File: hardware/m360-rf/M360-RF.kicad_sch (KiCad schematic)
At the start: 5 parts, among them J1 M360-RF 2x5, J2 SMA borda, U1 RFM95W-915S2

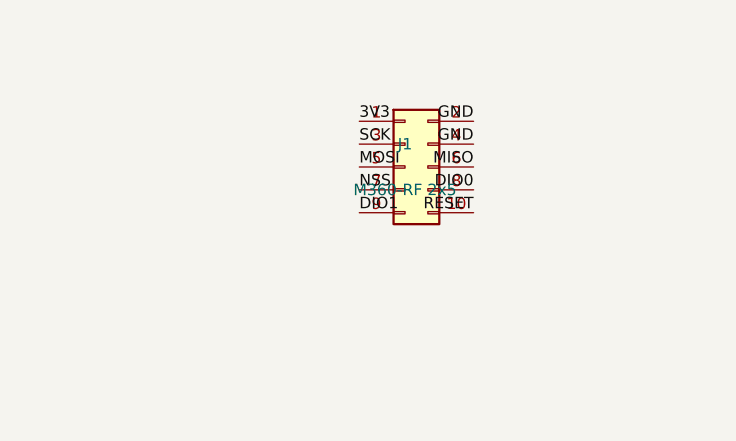
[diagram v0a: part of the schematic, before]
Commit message: feat(hardware): layout da placa do mezanino M360-RF
Placa de 34,2 x 23 mm, 2 camadas, 1,6 mm. RFM95W no centro; header 2x5 na face de baixo, à esquerda; SMA Samtec na borda direita, alinhado ao pino ANA. Trilha de RF coplanar com terra (1,25 mm, gap 0,2 mm, ~5 mm). SPI reto até a coluna de dentro do header; DIO1, DIO0 e 3V3 contornam o rádio por cima, em F.Cu, sem cruzamentos. GND nas duas faces com 17 vias de costura, nenhuma sob o módulo. Referências de C1, C2 e J2 ocultas na serigrafia.

Pinagem do header reordenada para o layout (MISO/MOSI/SCK/NSS/RESET na coluna ímpar, DIO1/DIO0/3V3/GND/GND na par); esquemático religado e ERC sem violações. DRC do kicad-cli: 0 violações, 0 itens desconectados, 0 divergências com o esquemático. ARQUITETURA_FAMILIA.md: nova pinagem e interface mecânica do mezanino para os carriers.

Co-Authored-By: Claude Opus 5 (1M context) <noreply@anthropic.com>

Claude-Session: https://claude.ai/code/session_01G3CpSsqAsoKgMUYE5MhRV7
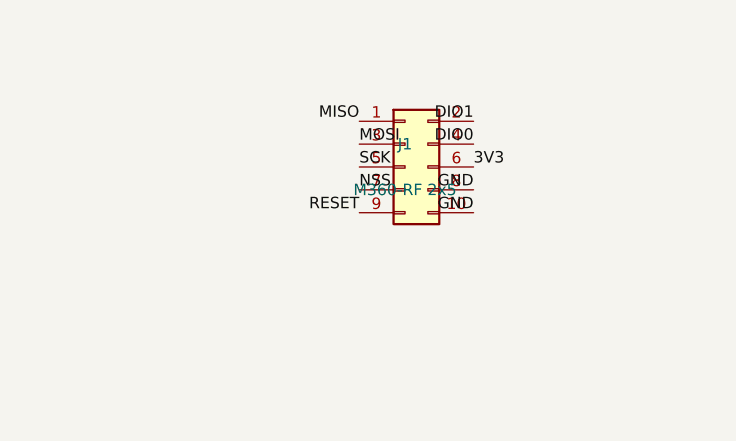
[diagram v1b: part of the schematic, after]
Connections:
- net 3V3: now also J1.6 (Pin_6); no longer J1.1 (Pin_1)
- net DIO0: now also J1.4 (Pin_4); no longer J1.8 (Pin_8)
- net DIO1: now also J1.2 (Pin_2); no longer J1.9 (Pin_9)
- net GND: now also J1.10 (Pin_10), J1.8 (Pin_8); no longer J1.2 (Pin_2), J1.4 (Pin_4)
- net MISO: now also J1.1 (Pin_1); no longer J1.6 (Pin_6)
- net MOSI: now also J1.3 (Pin_3); no longer J1.5 (Pin_5)
- net RESET: now also J1.9 (Pin_9); no longer J1.10 (Pin_10)
- net SCK: now also J1.5 (Pin_5); no longer J1.3 (Pin_3)
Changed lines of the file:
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@@
 			)
 		)
-    (property "MPN" "RFM95W-915S2" (at 110.49 90.17 0)
-      (effects (font (size 1.27 1.27)) (hide yes))
-    )
-    (property "Manufacturer" "HopeRF" (at 110.49 90.17 0)
-      (effects (font (size 1.27 1.27)) (hide yes))
-    )
-    (property "Montagem" "Manual: modulo HopeRF do estoque proprio, nao montar na PCBA" (at 110.49 90.17 0)
-      (effects (font (size 1.27 1.27)) (hide yes))
-    )
+		(property "MPN" "RFM95W-915S2"
+			(at 110.49 90.17 0)
+			(effects
+				(font
+					(size 1.27 1.27)
+				)
+				(hide yes)
+			)
+		)
+		(property "Manufacturer" "HopeRF"
+			(at 110.49 90.17 0)
+			(effects
+				(font
+					(size 1.27 1.27)
+				)
+				(hide yes)
+			)
+		)
+		(property "Montagem" "Manual: modulo HopeRF do estoque proprio, nao montar na PCBA"
+			(at 110.49 90.17 0)
+			(effects
+				(font
+					(size 1.27 1.27)
+				)
+				(hide yes)
+			)
+		)
 		(pin "1"
 		)
@@
 			)
 		)
-    (property "LCSC" "C492422" (at 175.26 90.17 0)
-      (effects (font (size 1.27 1.27)) (hide yes))
-    )
-    (property "Montagem" "Manual: header THT soldado apos a PCBA" (at 175.26 90.17 0)
-      (effects (font (size 1.27 1.27)) (hide yes))
-    )
+		(property "LCSC" "C492422"
+			(at 175.26 90.17 0)
+			(effects
+				(font
+					(size 1.27 1.27)
+				)
+				(hide yes)
+			)
+		)
+		(property "Montagem" "Manual: header THT soldado apos a PCBA"
+			(at 175.26 90.17 0)
+			(effects
+				(font
+					(size 1.27 1.27)
+				)
+				(hide yes)
+			)
+		)
 		(pin "1"
 		)
@@
 			)
 		)
-    (property "LCSC" "C5199907" (at 59.69 85.09 0)
-      (effects (font (size 1.27 1.27)) (hide yes))
-    )
-    (property "MPN" "SMA-J-P-H-ST-EM1" (at 59.69 85.09 0)
-      (effects (font (size 1.27 1.27)) (hide yes))
-    )
-    (property "Manufacturer" "Samtec" (at 59.69 85.09 0)
-      (effects (font (size 1.27 1.27)) (hide yes))
-    )
+		(property "LCSC" "C5199907"
+			(at 59.69 85.09 0)
+			(effects
+				(font
+					(size 1.27 1.27)
+				)
+				(hide yes)
+			)
+		)
+		(property "MPN" "SMA-J-P-H-ST-EM1"
+			(at 59.69 85.09 0)
+			(effects
+				(font
+					(size 1.27 1.27)
+				)
+				(hide yes)
+			)
+		)
+		(property "Manufacturer" "Samtec"
+			(at 59.69 85.09 0)
+			(effects
+				(font
+					(size 1.27 1.27)
+				)
+				(hide yes)
+			)
+		)
 		(pin "1"
 		)
@@
 			)
 		)
-    (property "LCSC" "C14663" (at 134.62 129.54 0)
-      (effects (font (size 1.27 1.27)) (hide yes))
-    )
+		(property "LCSC" "C14663"
+			(at 134.62 129.54 0)
+			(effects
+				(font
+					(size 1.27 1.27)
+				)
+				(hide yes)
+			)
+		)
 		(pin "1"
 		)
@@
 			)
 		)
-    (property "LCSC" "C45783" (at 149.86 129.54 0)
-      (effects (font (size 1.27 1.27)) (hide yes))
-    )
+		(property "LCSC" "C45783"
+			(at 149.86 129.54 0)
+			(effects
+				(font
+					(size 1.27 1.27)
+				)
+				(hide yes)
+			)
+		)
 		(pin "1"
 		)
@@
 		)
 	)
+	(label "RF_ANT"
+		(at 54.61 85.09 0)
+		(effects
+			(font
+				(size 1.27 1.27)
+			)
+			(justify left bottom)
+		)
+	)
+	(label "GND"
+		(at 59.69 90.17 90)
+		(effects
+			(font
+				(size 1.27 1.27)
+			)
+			(justify left bottom)
+		)
+	)
 	(label "3V3"
-		(at 170.17999999999998 85.09 0)
-		(effects
-			(font
-				(size 1.27 1.27)
-			)
-			(justify left bottom)
+		(at 134.62 125.72999999999999 270)
+		(effects
+			(font
+				(size 1.27 1.27)
+			)
+			(justify right bottom)
 		)
 	)
 	(label "GND"
+		(at 134.62 133.35 90)
+		(effects
+			(font
+				(size 1.27 1.27)
+			)
+			(justify left bottom)
+		)
+	)
+	(label "3V3"
+		(at 149.86 125.72999999999999 270)
+		(effects
+			(font
+				(size 1.27 1.27)
+			)
+			(justify right bottom)
+		)
+	)
+	(label "GND"
+		(at 149.86 133.35 90)
+		(effects
+			(font
+				(size 1.27 1.27)
+			)
+			(justify left bottom)
+		)
+	)
+	(label "3V3"
+		(at 190.5 129.54 90)
+		(effects
+			(font
+				(size 1.27 1.27)
+			)
+			(justify left bottom)
+		)
+	)
+	(label "GND"
+		(at 204.47 129.54 90)
+		(effects
+			(font
+				(size 1.27 1.27)
+			)
+			(justify left bottom)
+		)
+	)
+	(no_connect
+		(at 123.19 87.63)
+	)
+	(no_connect
+		(at 123.19 92.71000000000001)
+	)
+	(no_connect
+		(at 123.19 90.17)
+	)
+	(no_connect
+		(at 123.19 95.25)
+	)
+	(label "DIO1"
 		(at 182.88 85.09 180)
 		(effects
@@
 		)
 	)
+	(label "MOSI"
+		(at 170.17999999999998 87.63 0)
+		(effects
+			(font
+				(size 1.27 1.27)
+			)
+			(justify left bottom)
+		)
+	)
+	(label "DIO0"
+		(at 182.88 87.63 180)
+		(effects
+			(font
+				(size 1.27 1.27)
+			)
+			(justify right bottom)
+		)
+	)
 	(label "SCK"
-		(at 170.17999999999998 87.63 0)
-		(effects
-			(font
-				(size 1.27 1.27)
-			)
-			(justify left bottom)
-		)
-	)
-	(label "GND"
-		(at 182.88 87.63 180)
-		(effects
-			(font
-				(size 1.27 1.27)
-			)
-			(justify right bottom)
-		)
-	)
-	(label "MOSI"
 		(at 170.17999999999998 90.17 0)
 		(effects
@@
 			)
 			(justify left bottom)
-		)
-	)
-	(label "MISO"
-		(at 182.88 90.17 180)
-		(effects
-			(font
-				(size 1.27 1.27)
-			)
-			(justify right bottom)
 		)
 	)
@@
 		)
 	)
-	(label "DIO0"
+	(label "GND"
 		(at 182.88 92.71000000000001 180)
 		(effects
@@
 		)
 	)
-	(label "DIO1"
-		(at 170.17999999999998 95.25 0)
+	(label "GND"
+		(at 182.88 95.25 180)
+		(effects
+			(font
+				(size 1.27 1.27)
+			)
+			(justify right bottom)
+		)
+	)
+	(label "MISO"
+		(at 170.17999999999998 85.09 180)
+		(effects
+			(font
+				(size 1.27 1.27)
+			)
+			(justify right bottom)
+		)
+	)
+	(label "3V3"
+		(at 182.88 90.17 0)
 		(effects
 			(font
@@
 	)
 	(label "RESET"
-		(at 182.88 95.25 180)
-		(effects
-			(font
-				(size 1.27 1.27)
-			)
-			(justify right bottom)
-		)
-	)
-	(label "RF_ANT"
-		(at 54.61 85.09 0)
-		(effects
-			(font
-				(size 1.27 1.27)
-			)
-			(justify left bottom)
-		)
-	)
-	(label "GND"
-		(at 59.69 90.17 90)
-		(effects
-			(font
-				(size 1.27 1.27)
-			)
-			(justify left bottom)
-		)
-	)
-	(label "3V3"
-		(at 134.62 125.72999999999999 270)
-		(effects
-			(font
-				(size 1.27 1.27)
-			)
-			(justify right bottom)
-		)
-	)
-	(label "GND"
-		(at 134.62 133.35 90)
-		(effects
-			(font
-				(size 1.27 1.27)
-			)
-			(justify left bottom)
-		)
-	)
-	(label "3V3"
-		(at 149.86 125.72999999999999 270)
-		(effects
-			(font
-				(size 1.27 1.27)
-			)
-			(justify right bottom)
-		)
-	)
-	(label "GND"
-		(at 149.86 133.35 90)
-		(effects
-			(font
-				(size 1.27 1.27)
-			)
-			(justify left bottom)
-		)
-	)
-	(label "3V3"
-		(at 190.5 129.54 90)
-		(effects
-			(font
-				(size 1.27 1.27)
-			)
-			(justify left bottom)
-		)
-	)
-	(label "GND"
-		(at 204.47 129.54 90)
-		(effects
-			(font
-				(size 1.27 1.27)
-			)
-			(justify left bottom)
-		)
-	)
-	(no_connect
-		(at 123.19 87.63)
-	)
-	(no_connect
-		(at 123.19 92.71000000000001)
-	)
-	(no_connect
-		(at 123.19 90.17)
-	)
-	(no_connect
-		(at 123.19 95.25)
+		(at 170.17999999999998 95.25 180)
+		(effects
+			(font
+				(size 1.27 1.27)
+			)
+			(justify right bottom)
+		)
 	)
 	(sheet_instances

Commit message: feat(hardware): arquivos de fabricação da M360-RF
- U1 (RFM95W) e J1 (header 2x5, face de baixo) marcados como solda manual,
  fora do BOM e da posição; netdiff e paridade idênticos
- fabricacao/: C1, C2 e o SMA de borda J2, todos com LCSC
- §8: lista de solda manual das quatro placas

ERC 0, DRC --severity-all 0/0.

Co-Authored-By: Claude Opus 5 (1M context) <noreply@anthropic.com>
Claude-Session: https://claude.ai/code/session_012t7RkcrXvvpDVjKVimNu18
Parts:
- J1, U1: now left out of the parts list
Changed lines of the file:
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@@
 		(body_style 1)
 		(exclude_from_sim no)
-		(in_bom yes)
+		(in_bom no)
 		(on_board yes)
-		(in_pos_files yes)
+		(in_pos_files no)
 		(dnp no)
 		(property "Reference" "U1"
@@
 		(body_style 1)
 		(exclude_from_sim no)
-		(in_bom yes)
+		(in_bom no)
 		(on_board yes)
-		(in_pos_files yes)
+		(in_pos_files no)
 		(dnp no)
 		(property "Reference" "J1"
